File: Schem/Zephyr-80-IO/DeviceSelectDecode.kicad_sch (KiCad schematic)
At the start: 29 parts, among them SW3 SW_Coded_SH-7070, SW4 SW_Coded_SH-7070, SW5 SW_Coded_SH-7070, SW6 SW_Coded_SH-7030, SW7 SW_Coded_SH-7030, U4 74HC688, U5 74HC688, U6 74HC688, U7 74HC244

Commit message: Completed the IO Controller schematic and PCB layout for the Zephyr-80 project. This includes the design of the Baud Clock, CPU Address Decoding, Console Port, Device Select Decode, GPIO User Serial, and the main IO Controller schematics. Additionally, the PCB layout for the Zephyr-80 IO board has been created, along with the necessary library files and documentation for the control signal mapping.
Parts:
- added C20: 100n, Capacitor_SMD:C_0603_1608Metric, symbol Device:C
- added R27, R28, R29, R30: 4k7, Resistor_SMD:R_0603_1608Metric, symbol Device:R
- added SW6: SW_Coded_SH-7070, Button_Switch_THT:Nidec_Copal_SH-7010C, symbol Switch:SW_Coded_SH-7070
- added U12: 74HC688, Package_SO:TSSOP-20_4.4x6.5mm_P0.65mm, symbol 74xx:74HC688
- SW3, SW4, SW5: footprint (none) -> Button_Switch_THT:Nidec_Copal_SH-7010C
- U10: renamed from U5; footprint Package_SO:SOIC-20W_7.5x12.8mm_P1.27mm -> Package_SO:TSSOP-20_4.4x6.5mm_P0.65mm
- U11: renamed from U6; footprint Package_SO:SOIC-20W_7.5x12.8mm_P1.27mm -> Package_SO:TSSOP-20_4.4x6.5mm_P0.65mm
- U13: renamed from U7; footprint (none) -> Package_SO:TSSOP-20_4.4x6.5mm_P0.65mm; Manufacturer Code (none) -> SN74HC244PWR
- U9: renamed from U4; footprint Package_SO:SOIC-20W_7.5x12.8mm_P1.27mm -> Package_SO:TSSOP-20_4.4x6.5mm_P0.65mm; Manufacturer Code (none) -> SN74HC688PWR
- renumbered C12 to C16, C13 to C17, C14 to C18, C15 to C19, R8 to R15, R9 to R16, R10 to R17, R11 to R18, R12 to R19, R13 to R20, R14 to R21, R15 to R22, R16 to R23, R17 to R24, R18 to R25, R19 to R26, R20 to R31, R21 to R32, R22 to R33, R23 to R34, SW6 to SW7, SW7 to SW8
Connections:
- net +5V: now also C20.1, R27.1, R28.1, R29.1, R30.1, U12.20 (VCC)
- net CS0: now also U12.3 (R0)
- net CS1: now also U12.5 (R1)
- net CS2: now also U12.7 (R2)
- net CS3: now also U12.9 (R3)
- net GND: now also C20.2, SW6.C, U12.1 (G), U12.10 (GND), U12.11 (P4), U12.12 (R4), U12.13 (P5), U12.14 (R5), U12.15 (P6), U12.16 (R6), U12.17 (P7), U12.18 (R7)
- net ~{CE_SIO1}: now also U12.19 (P=R); no longer U10.19 (P=R)
- removed net SEL0: R15.2, R19.2, R23.2, SW3.1, SW4.1, SW5.1, U10.2 (P0), U11.2 (P0), U9.2 (P0)
- removed net SEL1: R16.2, R20.2, R24.2, SW3.2, SW4.2, SW5.2, U10.4 (P1), U11.4 (P1), U9.4 (P1)
- removed net SEL2: R17.2, R21.2, R25.2, SW3.4, SW4.4, SW5.4, U10.6 (P2), U11.6 (P2), U9.6 (P2)
- removed net SEL3: R18.2, R22.2, R26.2, SW3.8, SW4.8, SW5.8, U10.8 (P3), U11.8 (P3), U9.8 (P3)
- new net: R17.2, SW3.4, U9.6 (P2)
- new net: R21.2, SW4.4, U10.6 (P2)
- new net: R16.2, SW3.2, U9.4 (P1)
- new net: R30.2, SW6.8, U12.8 (P3)
- new net: R15.2, SW3.1, U9.2 (P0)
- new net: R25.2, SW5.4, U11.6 (P2)
- new net: R23.2, SW5.1, U11.2 (P0)
- new net: R18.2, SW3.8, U9.8 (P3)
- new net: R24.2, SW5.2, U11.4 (P1)
- new net: R26.2, SW5.8, U11.8 (P3)
- new net: R19.2, SW4.1, U10.2 (P0)
- new net: R20.2, SW4.2, U10.4 (P1)
- new net: R22.2, SW4.8, U10.8 (P3)
- new net: R29.2, SW6.4, U12.6 (P2)
- new net: R27.2, SW6.1, U12.2 (P0)
- new net: R28.2, SW6.2, U12.4 (P1)
- new net ~{CE_CTRL}: U10.19 (P=R)
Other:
- moved on the sheet: R15, R16, R17, R18, R19, R20, R21, R22, R23, R24, R25, R26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

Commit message: Added all the manufacturer part numbers to the KiCad schematics and PCB files. This will make it easier to order the parts for the project and ensure that the correct components are used. I also removed some of the old schematics that were no longer needed, such as the BaudClock, ConsolePort, DeviceSelectDecode, GPIOUserSerial, IO Controller, UserPorts, Video, and Z80HomeBrew schematics. These changes will help to streamline the design and make it easier to understand.
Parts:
- C16, C17, C18, C19, C20: MANUFACTURER_PART_NUMBER (none) -> C0603C104K5RACTU
- R15, R16, R17, R18, R19, R20, R21, R22, R23, R24, R25, R26, R27, R28, R29, R30, R31, R32, R33, R34: MANUFACTURER_PART_NUMBER (none) -> CRCW06034K70FKEA
- SW3, SW4, SW5, SW6: MANUFACTURER_PART_NUMBER (none) -> SH-7070TB
- SW7, SW8: MANUFACTURER_PART_NUMBER (none) -> 428527520909
- U10, U11, U12, U9: MANUFACTURER_PART_NUMBER (none) -> SN74HC688PWR
- U13: MANUFACTURER_PART_NUMBER (none) -> SN74HC244PWR

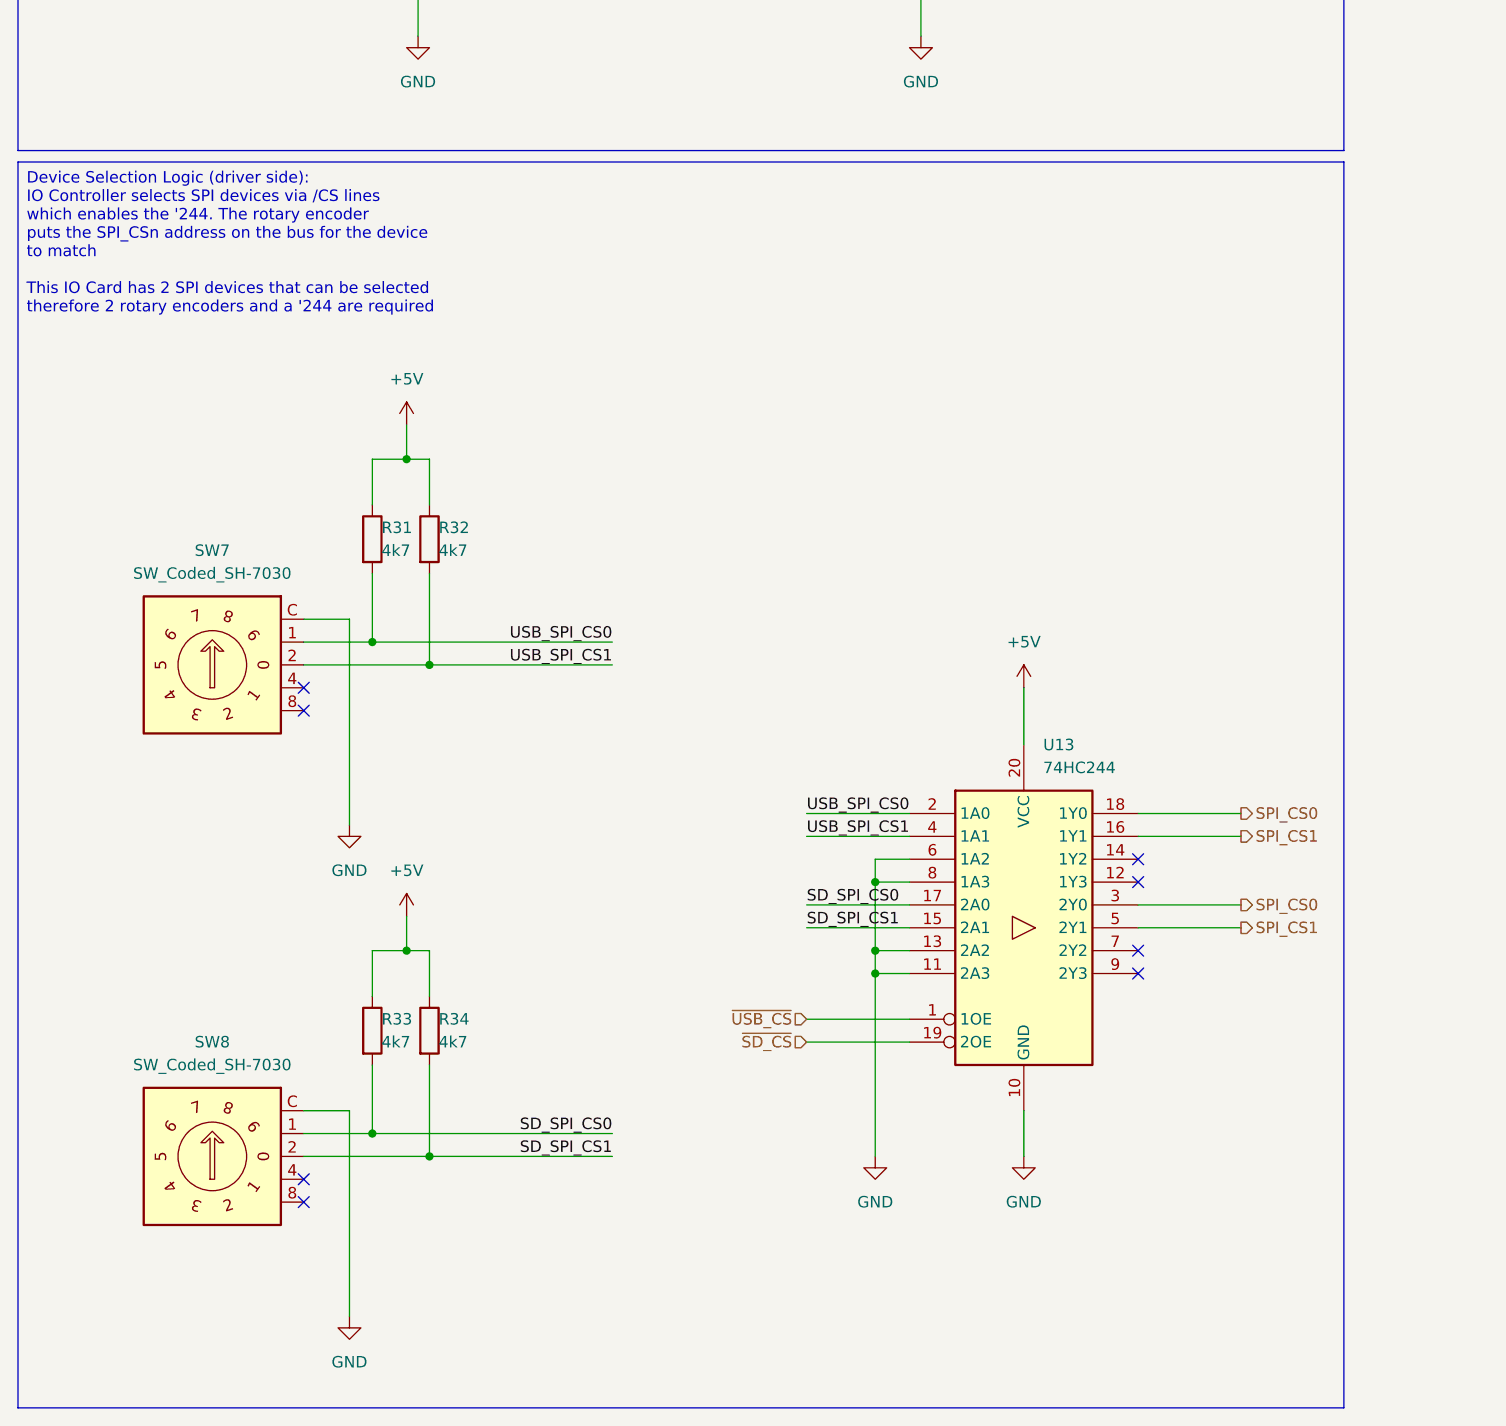
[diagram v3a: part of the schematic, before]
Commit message: Updated the IO Controller to properly support SDLC and SPI.
* Separated SPI1 and SPI2 and associated to the right pins.
      SPI1 is for devices (USB, SD Card and Controllers)
      SPI2 is for the SDLC controller (Z80 SIO1/A and B)

* Fixed the 1.27mm vs 2.54mm pin headers
* Fixed the power sequencing
* Fixed the pull ups
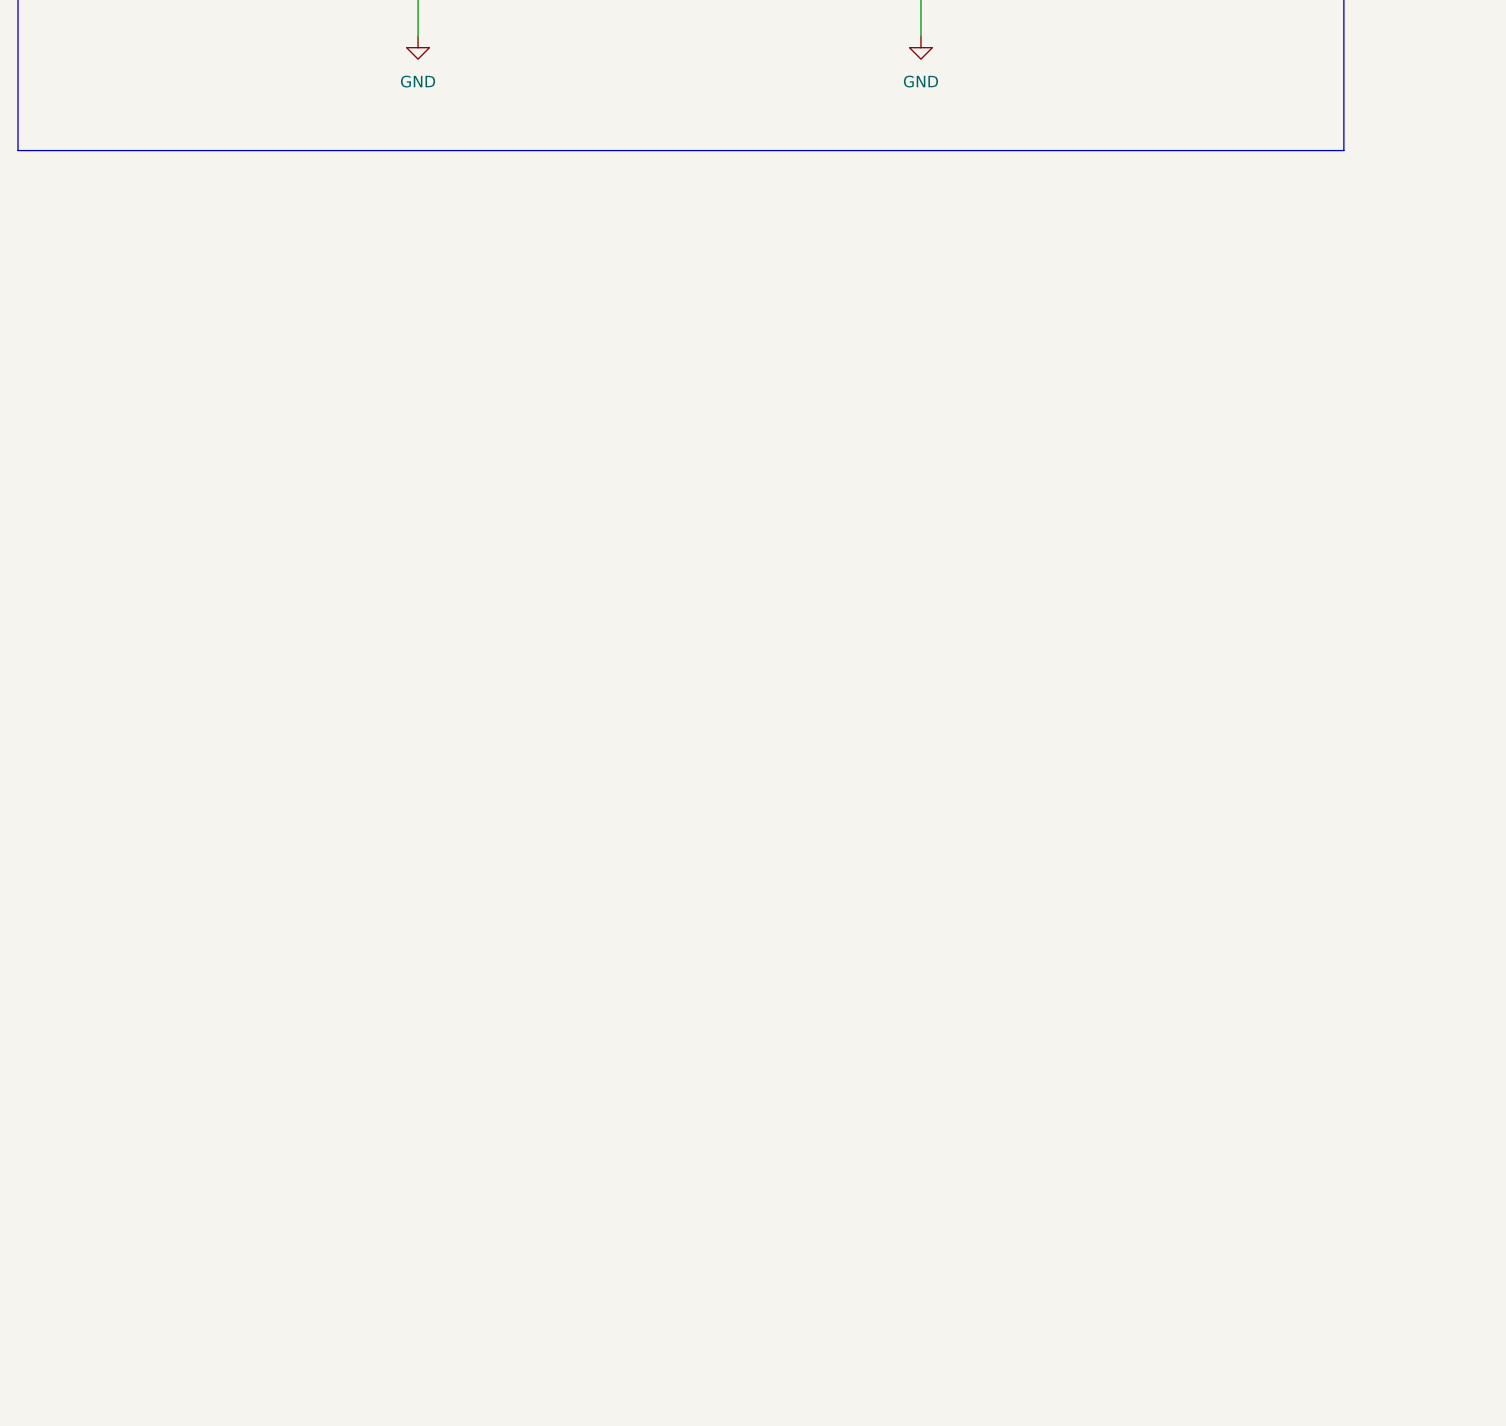
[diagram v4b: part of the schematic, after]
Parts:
- removed R31, R32, R33, R34: 4k7, Resistor_SMD:R_0603_1608Metric, symbol Device:R
- removed SW7, SW8: SW_Coded_SH-7030, Button_Switch_THT:Nidec_Copal_SH-7010C, symbol Switch:SW_Coded_SH-7030
- removed U13: 74HC244, Package_SO:TSSOP-20_4.4x6.5mm_P0.65mm, symbol 74xx:74HC244
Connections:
- no-connect marks 8 -> 0
